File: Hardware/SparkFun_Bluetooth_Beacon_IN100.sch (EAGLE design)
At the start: 24 parts, among them J3 Vertical Qwiic Connector, U1 IN100, Y1 CRYSTAL-26MHZSMD-3.2X2.5

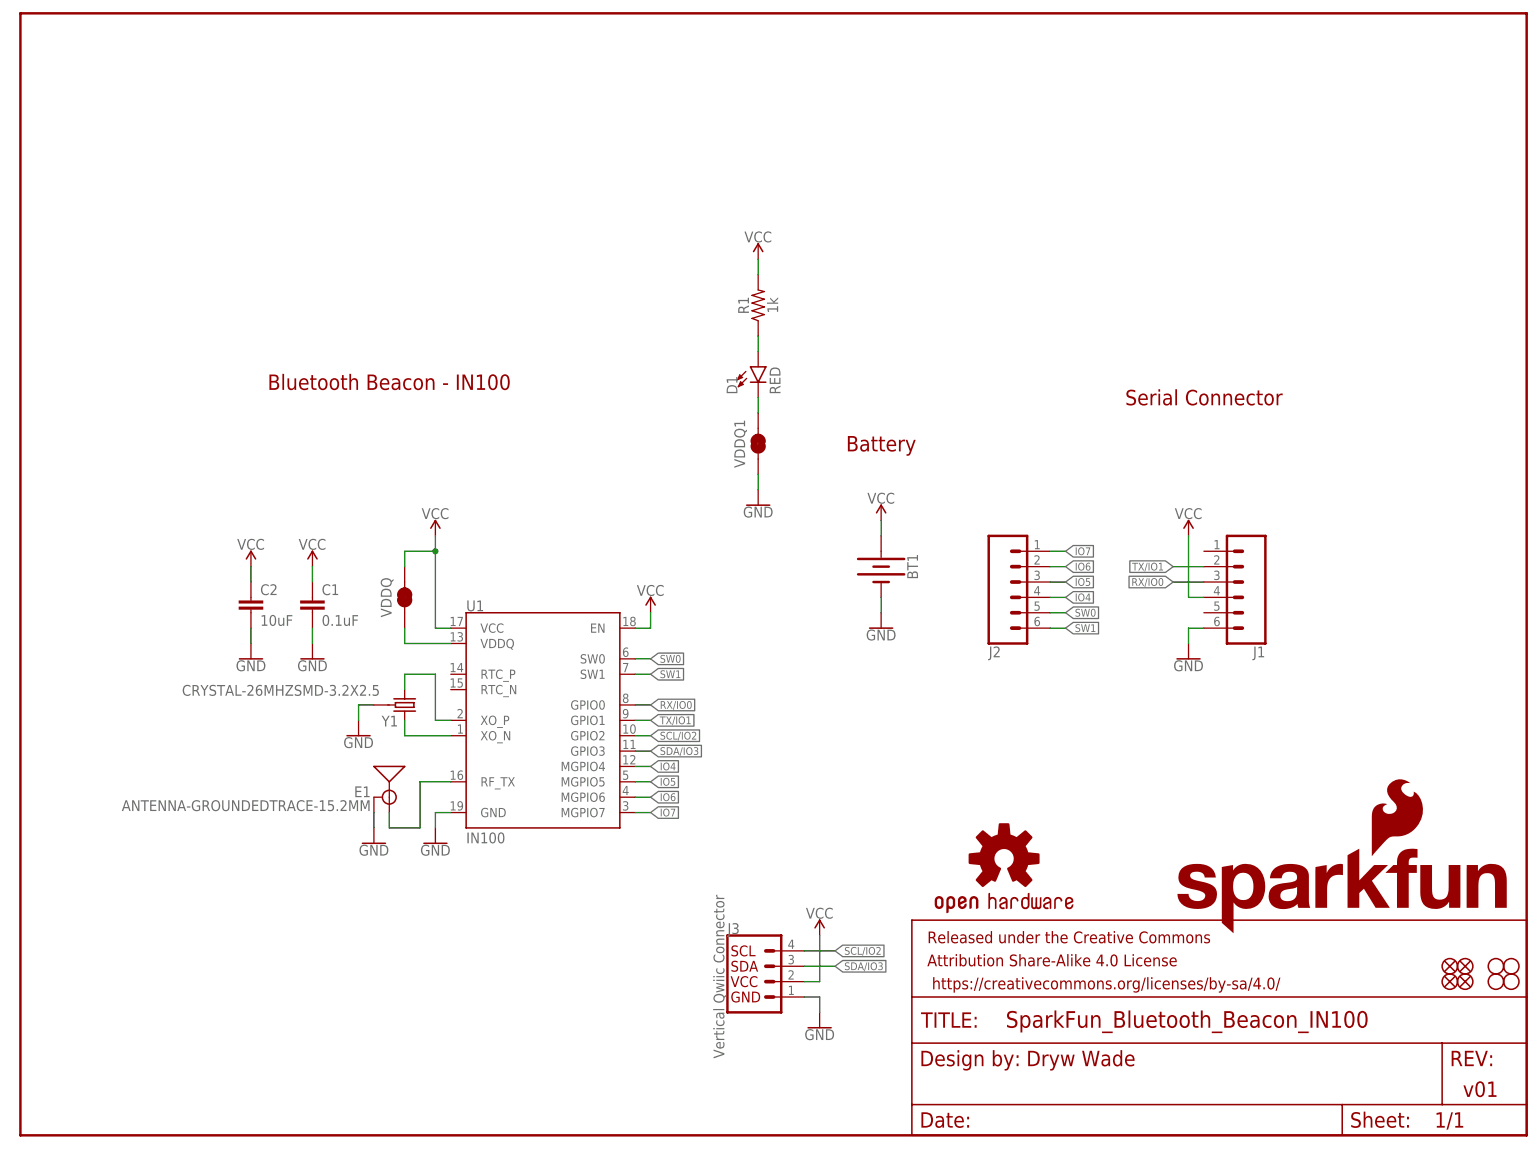
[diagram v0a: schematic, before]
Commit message: Pre-review cleanup
Clean up schematic
Add "programmed" checkbox to bottom silk
Add SW0 and SW1 to top silk
Update measures
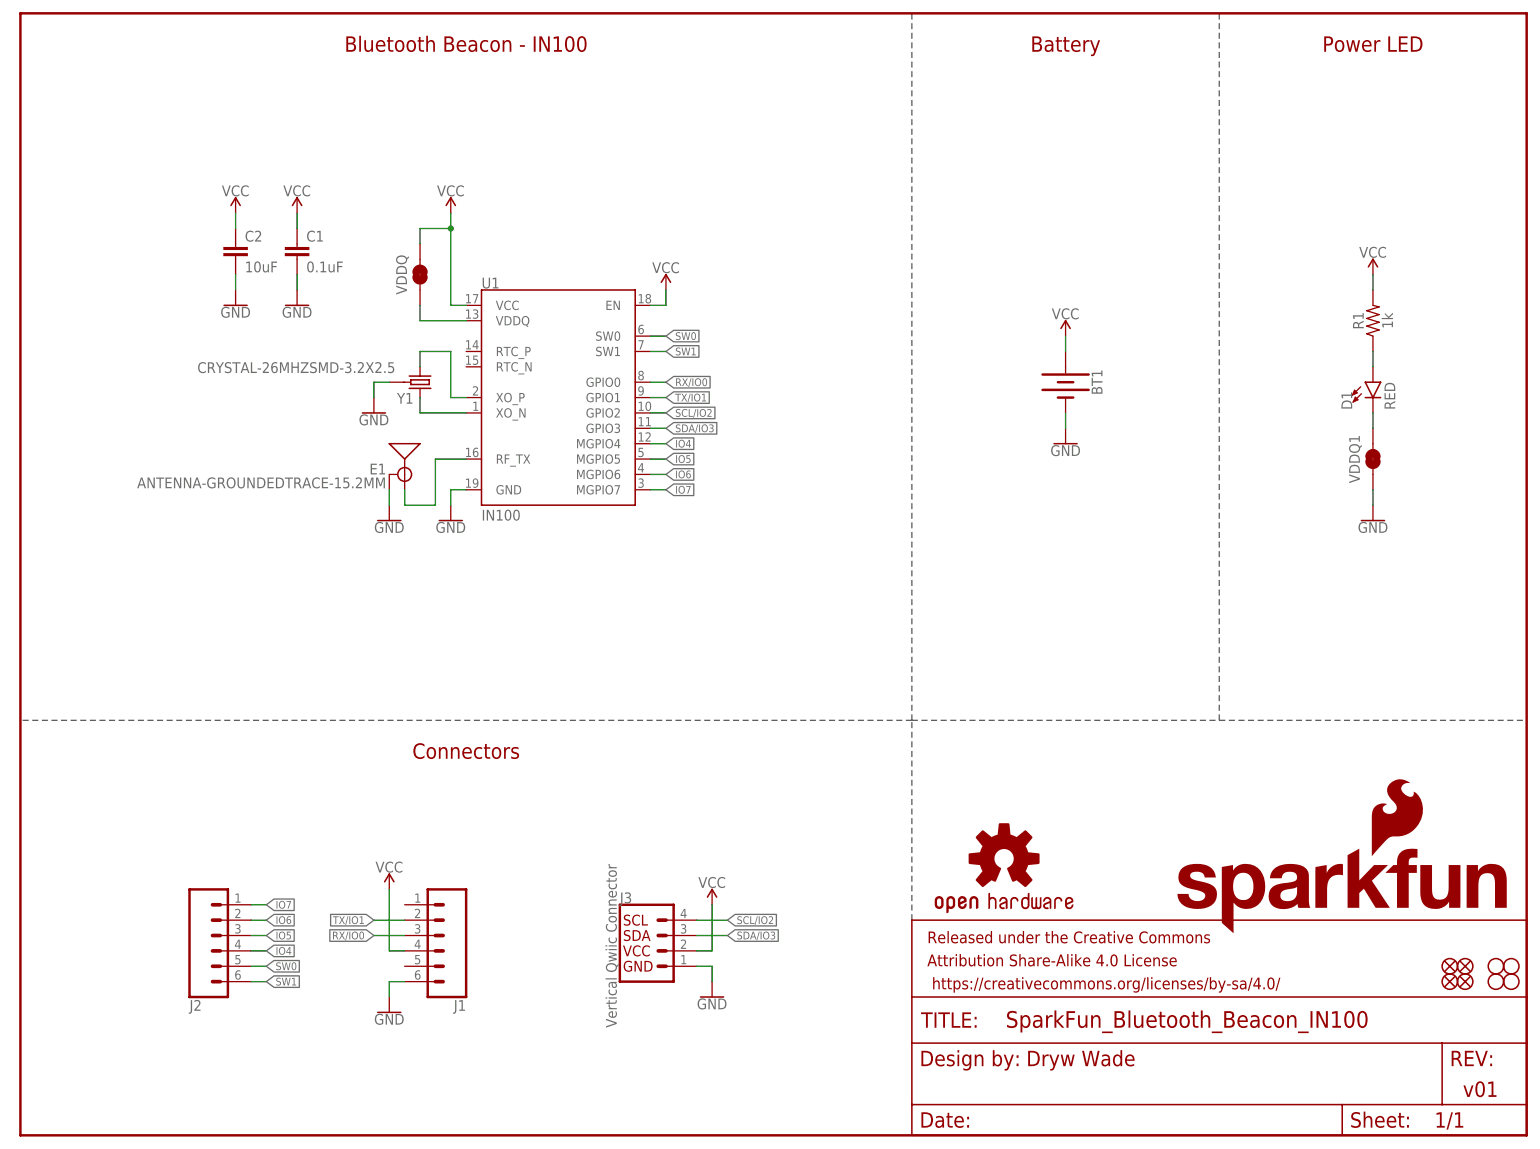
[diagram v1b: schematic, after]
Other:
- note added: "Connectors"
- note added: "Power LED"
- note removed: "Serial Connector"
- moved on the sheet: BT1, C1, C2, D1, E1, J1, J2, J3, R1, U1, VDDQ, VDDQ1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

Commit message: Design review updates
Add TX/RX labels to IN100 symbol
Add text to jumpers in schematic
Add VCC range to schematic
Rename PWR jumper in schematic
Increase crystal trace width to 10mil
Add more GND vias near RF trace
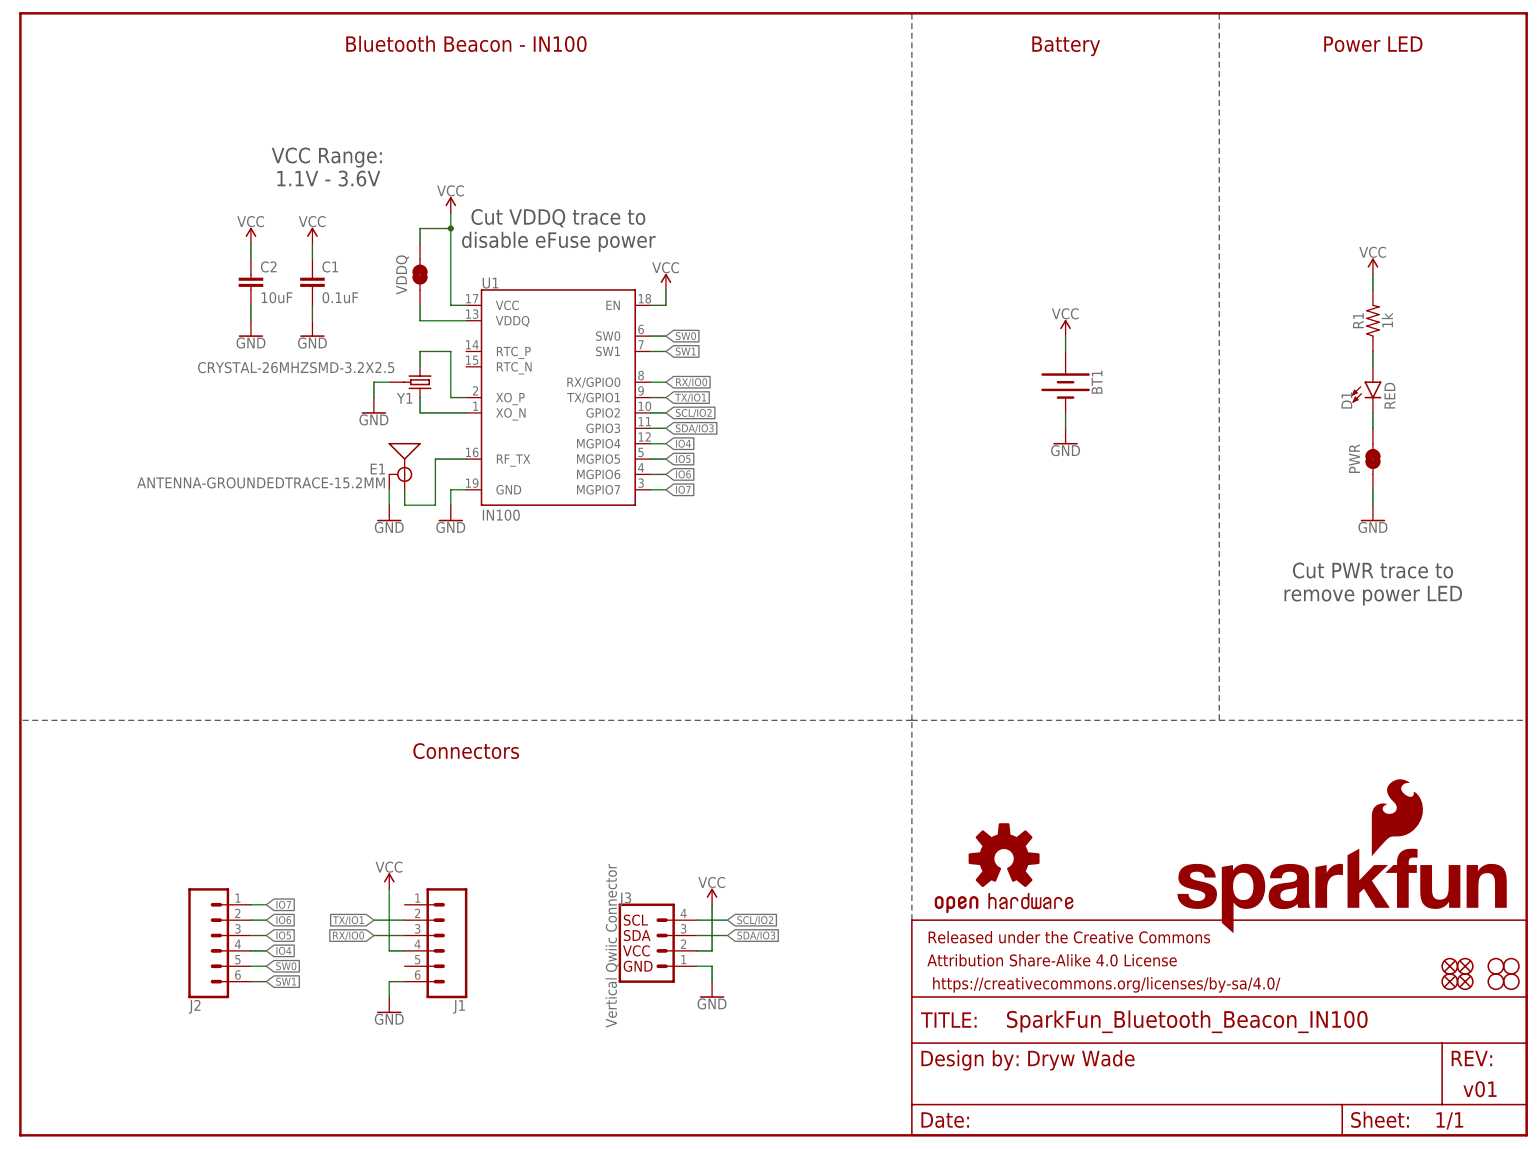
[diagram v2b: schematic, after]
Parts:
- renumbered VDDQ1 to PWR
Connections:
- net RX/IO0: now also U1.RX/GPIO0; no longer U1.GPIO0
- net TX/IO1: now also U1.TX/GPIO1; no longer U1.GPIO1
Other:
- note added: "Cut PWR trace to remove power LED"
- note added: "Cut VDDQ trace to disable eFuse power"
- note added: "VCC Range: 1.1V - 3.6V"
- moved on the sheet: C1, C2
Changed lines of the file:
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@@
 <part name="D1" library="SparkFun-LED" deviceset="LED-RED" device="0603" value="RED"/>
 <part name="R1" library="SparkFun-Resistors" deviceset="1KOHM" device="-0603-1/10W-1%" value="1k"/>
-<part name="VDDQ1" library="SparkFun-Jumpers" deviceset="JUMPER-SMT_2_NC_TRACE" device="_SILK" package3d_urn="urn:adsk.eagle:package:39281/1"/>
+<part name="PWR" library="SparkFun-Jumpers" deviceset="JUMPER-SMT_2_NC_TRACE" device="_SILK" package3d_urn="urn:adsk.eagle:package:39281/1"/>
 <part name="GND9" library="SparkFun-PowerSymbols" deviceset="GND" device=""/>
 <part name="SUPPLY8" library="SparkFun-PowerSymbols" deviceset="VCC" device=""/>
@@
 <wire x1="147.32" y1="68.58" x2="147.32" y2="185.42" width="0.2032" layer="97" style="longdash"/>
 <wire x1="198.12" y1="68.58" x2="198.12" y2="185.42" width="0.2032" layer="97" style="longdash"/>
+<text x="223.52" y="91.44" size="2.54" layer="97" font="vector" align="center">Cut PWR trace to
+remove power LED</text>
+<text x="88.9" y="149.86" size="2.54" layer="97" font="vector" align="center">Cut VDDQ trace to
+disable eFuse power</text>
+<text x="50.8" y="160.02" size="2.54" layer="97" font="vector" align="center">VCC Range:
+1.1V - 3.6V</text>
 </plain>
 <instances>
@@
 <attribute name="VALUE" x="58.42" y="119.126" size="1.778" layer="96" font="vector" align="top-center"/>
 </instance>
-<instance part="C1" gate="G$1" x="45.72" y="144.78" smashed="yes">
-<attribute name="NAME" x="47.244" y="147.701" size="1.778" layer="95" font="vector"/>
-<attribute name="VALUE" x="47.244" y="142.621" size="1.778" layer="96" font="vector"/>
-</instance>
-<instance part="GND4" gate="1" x="45.72" y="137.16" smashed="yes">
-<attribute name="VALUE" x="45.72" y="136.906" size="1.778" layer="96" font="vector" align="top-center"/>
+<instance part="C1" gate="G$1" x="48.26" y="139.7" smashed="yes">
+<attribute name="NAME" x="49.784" y="142.621" size="1.778" layer="95" font="vector"/>
+<attribute name="VALUE" x="49.784" y="137.541" size="1.778" layer="96" font="vector"/>
+</instance>
+<instance part="GND4" gate="1" x="48.26" y="132.08" smashed="yes">
+<attribute name="VALUE" x="48.26" y="131.826" size="1.778" layer="96" font="vector" align="top-center"/>
 </instance>
 <instance part="J1" gate="JP1" x="68.58" y="33.02" smashed="yes" rot="R180">
@@
 <attribute name="VALUE" x="172.72" y="134.874" size="1.778" layer="96" font="vector" align="bottom-center"/>
 </instance>
-<instance part="SUPPLY2" gate="G$1" x="45.72" y="152.4" smashed="yes">
-<attribute name="VALUE" x="45.72" y="155.194" size="1.778" layer="96" font="vector" align="bottom-center"/>
+<instance part="SUPPLY2" gate="G$1" x="48.26" y="147.32" smashed="yes">
+<attribute name="VALUE" x="48.26" y="150.114" size="1.778" layer="96" font="vector" align="bottom-center"/>
 </instance>
 <instance part="SUPPLY3" gate="G$1" x="71.12" y="152.4" smashed="yes">
@@
 <attribute name="VALUE" x="60.96" y="43.434" size="1.778" layer="96" font="vector" align="bottom-center"/>
 </instance>
-<instance part="C2" gate="G$1" x="35.56" y="144.78" smashed="yes">
-<attribute name="NAME" x="37.084" y="147.701" size="1.778" layer="95" font="vector"/>
-<attribute name="VALUE" x="37.084" y="142.621" size="1.778" layer="96" font="vector"/>
-</instance>
-<instance part="GND7" gate="1" x="35.56" y="137.16" smashed="yes">
-<attribute name="VALUE" x="35.56" y="136.906" size="1.778" layer="96" font="vector" align="top-center"/>
-</instance>
-<instance part="SUPPLY6" gate="G$1" x="35.56" y="152.4" smashed="yes">
-<attribute name="VALUE" x="35.56" y="155.194" size="1.778" layer="96" font="vector" align="bottom-center"/>
+<instance part="C2" gate="G$1" x="38.1" y="139.7" smashed="yes">
+<attribute name="NAME" x="39.624" y="142.621" size="1.778" layer="95" font="vector"/>
+<attribute name="VALUE" x="39.624" y="137.541" size="1.778" layer="96" font="vector"/>
+</instance>
+<instance part="GND7" gate="1" x="38.1" y="132.08" smashed="yes">
+<attribute name="VALUE" x="38.1" y="131.826" size="1.778" layer="96" font="vector" align="top-center"/>
+</instance>
+<instance part="SUPPLY6" gate="G$1" x="38.1" y="147.32" smashed="yes">
+<attribute name="VALUE" x="38.1" y="150.114" size="1.778" layer="96" font="vector" align="bottom-center"/>
 </instance>
 <instance part="J2" gate="JP1" x="33.02" y="33.02" smashed="yes" rot="MR180">
@@
 <attribute name="VALUE" x="225.044" y="134.62" size="1.778" layer="96" font="vector" rot="R90" align="top-center"/>
 </instance>
-<instance part="VDDQ1" gate="G$1" x="223.52" y="111.76" smashed="yes" rot="R90">
+<instance part="PWR" gate="G$1" x="223.52" y="111.76" smashed="yes" rot="R90">
 <attribute name="NAME" x="220.472" y="111.76" size="1.778" layer="95" font="vector" rot="R90" align="center"/>
 </instance>
@@
 <pinref part="GND4" gate="1" pin="GND"/>
 <pinref part="C1" gate="G$1" pin="2"/>
-<wire x1="45.72" y1="139.7" x2="45.72" y2="142.24" width="0.1524" layer="91"/>
+<wire x1="48.26" y1="134.62" x2="48.26" y2="137.16" width="0.1524" layer="91"/>
 </segment>
 <segment>
@@
 <segment>
 <pinref part="GND7" gate="1" pin="GND"/>
-<wire x1="35.56" y1="139.7" x2="35.56" y2="142.24" width="0.1524" layer="91"/>
+<wire x1="38.1" y1="134.62" x2="38.1" y2="137.16" width="0.1524" layer="91"/>
 <pinref part="C2" gate="G$1" pin="2"/>
 </segment>
@@
 <segment>
 <pinref part="GND9" gate="1" pin="GND"/>
-<pinref part="VDDQ1" gate="G$1" pin="1"/>
+<pinref part="PWR" gate="G$1" pin="1"/>
 <wire x1="223.52" y1="104.14" x2="223.52" y2="106.68" width="0.1524" layer="91"/>
 </segment>
@@
 <pinref part="SUPPLY2" gate="G$1" pin="VCC"/>
 <pinref part="C1" gate="G$1" pin="1"/>
-<wire x1="45.72" y1="152.4" x2="45.72" y2="149.86" width="0.1524" layer="91"/>
+<wire x1="48.26" y1="147.32" x2="48.26" y2="144.78" width="0.1524" layer="91"/>
 </segment>
 <segment>
@@
 <segment>
 <pinref part="SUPPLY6" gate="G$1" pin="VCC"/>
-<wire x1="35.56" y1="152.4" x2="35.56" y2="149.86" width="0.1524" layer="91"/>
+<wire x1="38.1" y1="147.32" x2="38.1" y2="144.78" width="0.1524" layer="91"/>
 <pinref part="C2" gate="G$1" pin="1"/>
 </segment>
@@
 </segment>
 <segment>
-<pinref part="U1" gate="G$1" pin="GPIO1"/>
+<pinref part="U1" gate="G$1" pin="TX/GPIO1"/>
 <wire x1="104.14" y1="121.92" x2="106.68" y2="121.92" width="0.1524" layer="91"/>
 <label x="106.68" y="121.92" size="1.27" layer="95" font="vector" xref="yes"/>
@@
 </segment>
 <segment>
-<pinref part="U1" gate="G$1" pin="GPIO0"/>
+<pinref part="U1" gate="G$1" pin="RX/GPIO0"/>
 <wire x1="104.14" y1="124.46" x2="106.68" y2="124.46" width="0.1524" layer="91"/>
 <label x="106.68" y="124.46" size="1.27" layer="95" font="vector" xref="yes"/>
@@
 <net name="N$5" class="0">
 <segment>
-<pinref part="VDDQ1" gate="G$1" pin="2"/>
+<pinref part="PWR" gate="G$1" pin="2"/>
 <pinref part="D1" gate="G$1" pin="C"/>
 <wire x1="223.52" y1="119.38" x2="223.52" y2="116.84" width="0.1524" layer="91"/>
@@
 </drawing>
 <compatibility>
+<note version="6.3" minversion="6.2.2" severity="warning">
+Since Version 6.2.2 text objects can contain more than one line,
+which will not be processed correctly with this version.
+</note>
 <note version="8.3" severity="warning">
 Since Version 8.3, EAGLE supports URNs for individual library
